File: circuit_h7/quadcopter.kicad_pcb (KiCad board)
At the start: 4 copper layers, 37.5 x 37.5 mm, 108 parts, among them J1 Conn_01x04_Male, J10 Conn_01x01_Female, J11 Conn_01x04_Male, J12 Conn_01x04_Male, J13 Conn_01x01_Female, J14 Conn_01x01_Female, J16 Conn_01x01_Female, J17 Conn_01x01_Female, J18 USB_C_Receptacle_USB2.0, J19 Conn_01x08_Male, J2 Conn_01x01_Female, J21 Conn_01x01_Female, J22 Conn_01x01_Female, J23 Conn_01x01_Female, J24 Conn_01x01_Female, J25 Conn_01x01_Female, J26 Conn_01x01_Female, J28 Conn_01x01_Female, J29 Conn_01x01_Female, J3 Conn_01x01_Female, J30 Conn_01x01_Female, J31 Conn_01x01_Female, J32 Conn_01x01_Female, J33 Conn_01x01_Female, J37 Conn_01x01_Female, J4 Conn_01x01_Female, J40 Conn_01x01_Female, J41 Conn_01x01_Female, J42 Conn_01x01_Female, J43 Conn_01x01_Female, J44 Conn_01x01_Female, J45 Conn_01x01_Female, J47 Conn_01x01_Female, J48 Conn_01x01_Female, J49 Conn_01x01_Female, J5 Conn_Coaxial, J50 Conn_01x01_Female, J6 Conn_01x06_Male, J7 Conn_01x01_Female, J8 Conn_01x01_Female, J9 Conn_01x01_Female, SW1 SW_DIP_x01, U1 STM32H723VGH6, U2 ICM-42605, U3 DPS310, U4 3V3, U5 EUP3458 1.2A, 30V max input, 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, U6 2450FM07D0034T, U7 W25Q80DVUXIE TR (16M), U8 SX1281, U9 5v, 500mA, Y1 16M, Y2 52Mhz, 12pF

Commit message: More work on routing
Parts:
- added J15: Conn_01x01_Female, TestPoint:TestPoint_Pad_2.0x2.0mm, B.Cu at (138.8, 97.2)
- moved R16 34.8 mm to (147.5, 85.2)
- moved R18 33.5 mm to (147.5, 86.2)
- moved R14 25.2 mm to (150.2, 95.5)
- moved R13 23.7 mm to (152.2, 95.5), turned to 0 degrees
- moved J12 21.1 mm to (141.6, 75.4)
- moved C2 16.2 mm to (147.3, 90.6), turned to -90 degrees
- moved U3 15.3 mm to (144.8, 90.6), turned to 0 degrees
- moved C5 15.1 mm to (142.3, 90.6), turned to 90 degrees
- moved J32 5.13 mm to (135.2, 97.2)
- moved C10 0.10 mm to (134.0, 78.6)
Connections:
- U1 pad G4: /IMU_INTERRUPT -> /CS_IMU
- U1 pad K8: /CS_IMU -> /IMU_INTERRUPT
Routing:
- net +10V: track 18.8 -> 52.3 mm
- net /USB_DN: track 0.00 -> 22.6 mm, vias 0 -> 2
- net /USB_DP: track 0.00 -> 21.5 mm, vias 0 -> 2
- net /BATT_DIV: track 0.00 -> 19.9 mm, vias 0 -> 2
- net /IMU_pwr: track 13.9 -> 32.7 mm, vias 0 -> 1
- net /UART3_RX: track 1.10 -> 16.1 mm
- net /BOOT0: track 0.00 -> 14.4 mm, vias 0 -> 2
- net /CUR_DIV: track 0.00 -> 13.8 mm, vias 0 -> 2
- net +3V3: track 17.4 -> 31.0 mm, vias 3 -> 10
- net /CS_ELRS: track 0.00 -> 13.4 mm, vias 0 -> 2
- net /ELRS_BUSY: track 0.00 -> 13.0 mm, vias 0 -> 2
- net GND: track 17.7 -> 30.0 mm, vias 8 -> 37
- net /SCL2: track 0.00 -> 12.2 mm, vias 0 -> 2
- net /SDA2: track 0.00 -> 10.9 mm, vias 0 -> 2
- net +5V: track 9.57 -> 19.0 mm, vias 2 -> 4
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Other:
- board text added: "I2C"

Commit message: More work on BF pid
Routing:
- net /UART2_RX: track 1.43 -> 20.0 mm, vias 1 -> 2
- net /UART2_TX: track 0.78 -> 14.9 mm, vias 1 -> 2
- net /IMU_pwr: track 32.7 -> 37.3 mm, vias 1 -> 2
- net GND: track 30.0 -> 33.7 mm, vias 37 -> 44
- net /USB_DN: track 22.6 -> 24.9 mm
- net /USB_DP: track 21.5 -> 23.7 mm
- net +3V3: track 31.0 -> 30.2 mm, vias 10 -> 12

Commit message: More work on board. Removed motor args from set power fns
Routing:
- net /UART1_RX: track 1.43 -> 57.1 mm, vias 1 -> 6
- net /UART4_TX: track 0.00 -> 31.4 mm, vias 0 -> 2
- net /UART4_RX: track 0.00 -> 26.3 mm, vias 0 -> 2
- net /SDA2: track 10.9 -> 28.5 mm, vias 2 -> 3
- net GND: track 33.7 -> 41.5 mm, vias 44 -> 52
- net +3V3: track 30.2 -> 35.5 mm, vias 12 -> 13
- net /MISO_2: track 14.1 -> 16.2 mm
- net +10V: track 52.3 -> 53.2 mm
- net /USB_DN: track 24.9 -> 24.2 mm

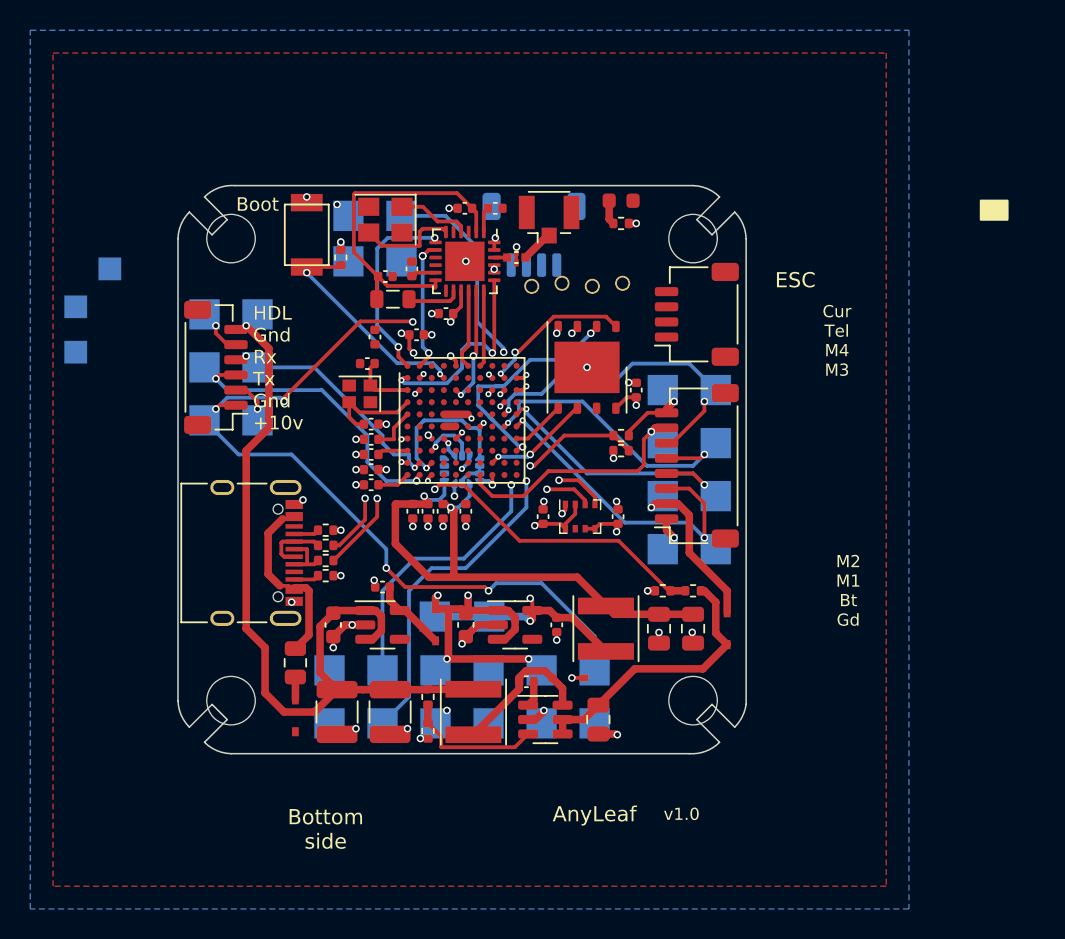
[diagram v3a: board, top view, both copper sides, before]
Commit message: Added link stats to preflight
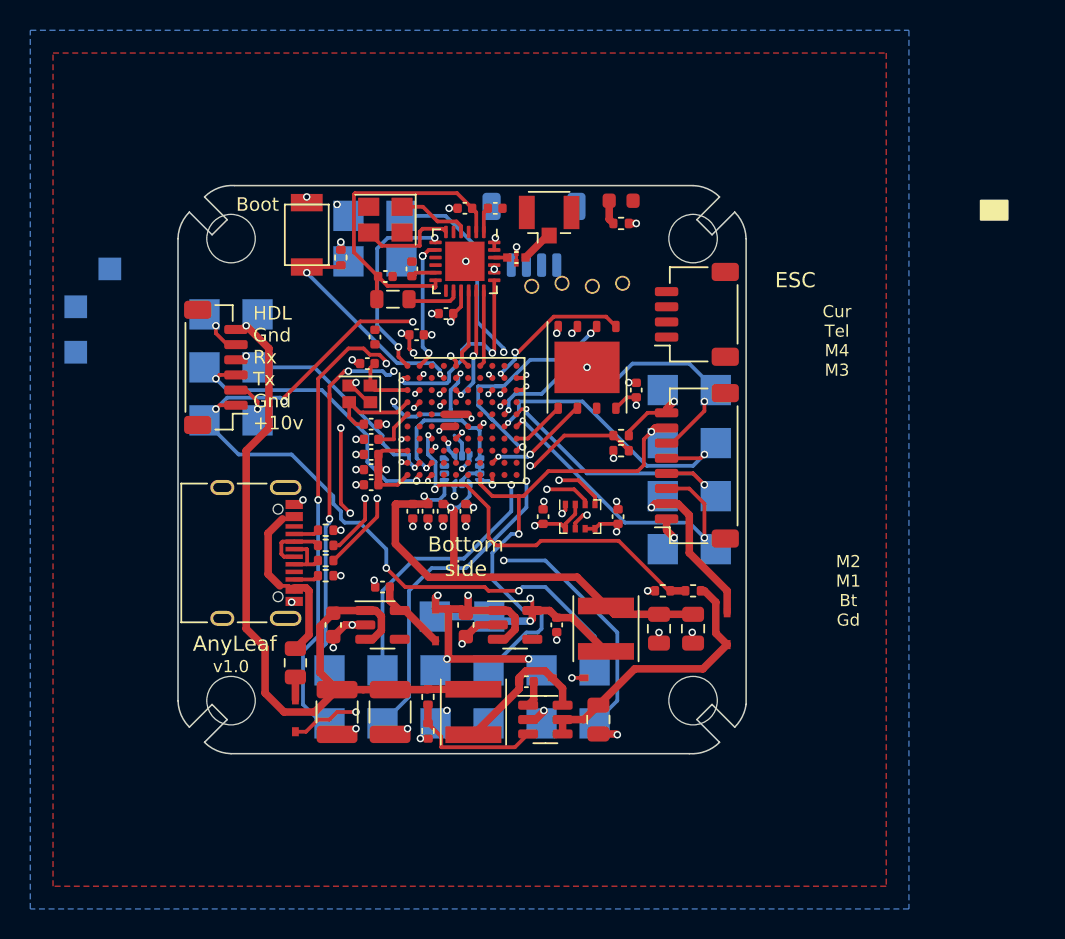
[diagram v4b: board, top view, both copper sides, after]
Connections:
- J14 pad 1: /UART5_RX -> /UART8_RX
- J2 pad 1: /UART5_TX -> /UART8_TX
- U1 pad C4: unconnected-(U1-PadC4) -> /UART8_TX
- U1 pad D4: unconnected-(U1-PadD4) -> /UART8_RX
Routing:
- net /UART1_TX: track 0.00 -> 45.6 mm, vias 0 -> 5
- net /UART8_TX: track 0.00 -> 35.5 mm, vias 0 -> 3
- net /UART8_RX: track 0.00 -> 28.6 mm, vias 0 -> 4
- net /UART3_RX: track 16.1 -> 32.4 mm, vias 1 -> 2
- net +5V: track 19.0 -> 31.0 mm, vias 4 -> 5
- net +3V3: track 35.5 -> 45.4 mm, vias 13 -> 16
- net /BATT_DIV: track 19.9 -> 25.1 mm
- net GND: track 41.5 -> 45.9 mm, vias 52 -> 55
- net /SCK_1: track 3.61 -> 1.90 mm

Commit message: H7 fixes
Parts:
- added C32: 12p, Capacitor_SMD:C_0402_1005Metric, F.Cu at (158.2, 65.0)
- added C33: 6.8p, Capacitor_SMD:C_0402_1005Metric, F.Cu at (158.3, 63.0)
- added C34: 1u 25v, Capacitor_SMD:C_0402_1005Metric, F.Cu at (147.8, 62.0)
- added C35: 100n, Capacitor_SMD:C_0402_1005Metric, F.Cu at (155.2, 67.0)
- added C36: 10u, Capacitor_SMD:C_0402_1005Metric, F.Cu at (155.4, 65.0)
- added C37: 1u 25v, Capacitor_SMD:C_0402_1005Metric, F.Cu at (146.2, 64.2)
- added D6: LED, LED_SMD:LED_0603_1608Metric, F.Cu at (151.2, 65.2)
- added J20: Conn_01x01_Female, TestPoint:TestPoint_Pad_1.0x1.0mm, B.Cu at (149.5, 77.8)
- added R6: 10k, Resistor_SMD:R_0402_1005Metric, F.Cu at (155.4, 63.0)
- added R9: 3.3k, Resistor_SMD:R_0402_1005Metric, F.Cu at (172.7, 70.2)
- added U10: ESP8285, Package_DFN_QFN:QFN-32-1EP_5x5mm_P0.5mm_EP3.45x3.45mm, F.Cu at (145.2, 76.2)
- added Y3: 40M, Crystal:Crystal_SMD_2016-4Pin_2.0x1.6mm, F.Cu at (150.8, 77.0)
- J1: value Conn_01x04_Male -> Conn_01x01_Female; footprint Connector_JST:JST_SH_SM04B-SRSS-TB_1x04-1MP_P1.00mm_Horizontal -> TestPoint:TestPoint_Pad_1.0x1.0mm; moved to B.Cu
- J11: footprint Connector_JST:JST_SH_SM04B-SRSS-TB_1x04-1MP_P1.00mm_Horizontal -> Connector_JST:JST_GH_SM04B-GHS-TB_1x04-1MP_P1.25mm_Horizontal
- J19: footprint Connector_JST:JST_SH_SM08B-SRSS-TB_1x08-1MP_P1.00mm_Horizontal -> Connector_JST:JST_GH_SM08B-GHS-TB_1x08-1MP_P1.25mm_Horizontal
- J6: footprint Connector_JST:JST_SH_BM06B-SRSS-TB_1x06-1MP_P1.00mm_Vertical -> Connector_JST:JST_GH_SM06B-GHS-TB_1x06-1MP_P1.25mm_Horizontal
- moved J12 38.7 mm to (110.8, 98.8)
- moved J1 3.35 mm to (149.5, 75.8), turned to 180 degrees
- moved U7 2.25 mm to (145.2, 83.0)
- moved R18 2.14 mm to (145.5, 87.0)
- moved J11 1.77 mm to (143.5, 72.2)
- moved R16 1.75 mm to (147.5, 87.0)
- moved J6 1.06 mm to (121.5, 81.5), turned to -90 degrees
- moved C23 0.35 mm to (148.8, 82.5)
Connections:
- J1 pad 1: /SCL1 -> /TX_ELRS
- U1 pad A1: /ELRS_BUSY -> unconnected-(U1-PadA1)
- U1 pad A2: /ELRS_DIO -> unconnected-(U1-PadA2)
- U1 pad A6: /MISO_3 -> unconnected-(U1-PadA6)
- U1 pad A7: /SCK_3 -> unconnected-(U1-PadA7)
- U1 pad B1: /CS_ELRS -> unconnected-(U1-PadB1)
- U1 pad C5: /MOSI_3 -> unconnected-(U1-PadC5)
- U8 pad 16: /MISO_3 -> /MISO_ELRS
- U8 pad 17: /MOSI_3 -> /MOSI_ELRS
- U8 pad 18: /SCK_3 -> /SCK_ELRS
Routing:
- net /SDA1: track 0.00 -> 14.4 mm, vias 0 -> 1
- net unconnected-(U1-PadA1): track 0.00 -> 13.0 mm, vias 0 -> 2
- net /ELRS_BUSY: track 13.0 -> 0.00 mm, vias 2 -> 0
- net /MISO_ELRS: track 0.00 -> 9.91 mm, vias 0 -> 3
- net /SCL1: track 0.00 -> 9.12 mm, vias 0 -> 1
- net /CS_ELRS: track 13.4 -> 4.66 mm
- net unconnected-(U1-PadA2): track 0.00 -> 8.68 mm, vias 0 -> 3
- net /ELRS_DIO: track 8.68 -> 0.00 mm, vias 3 -> 0
- net unconnected-(U1-PadB1): track 0.00 -> 8.57 mm, vias 0 -> 2
- net /CS_FLASH: track 10.2 -> 2.26 mm
- net /MOSI_3: track 7.77 -> 0.00 mm, vias 2 -> 0
- net /CUR_DIV: track 13.8 -> 7.26 mm
- net /MISO_2: track 16.2 -> 10.1 mm, vias 2 -> 1
- net /SCK_ELRS: track 0.00 -> 6.09 mm
- net /MOSI_ELRS: track 0.00 -> 5.71 mm
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
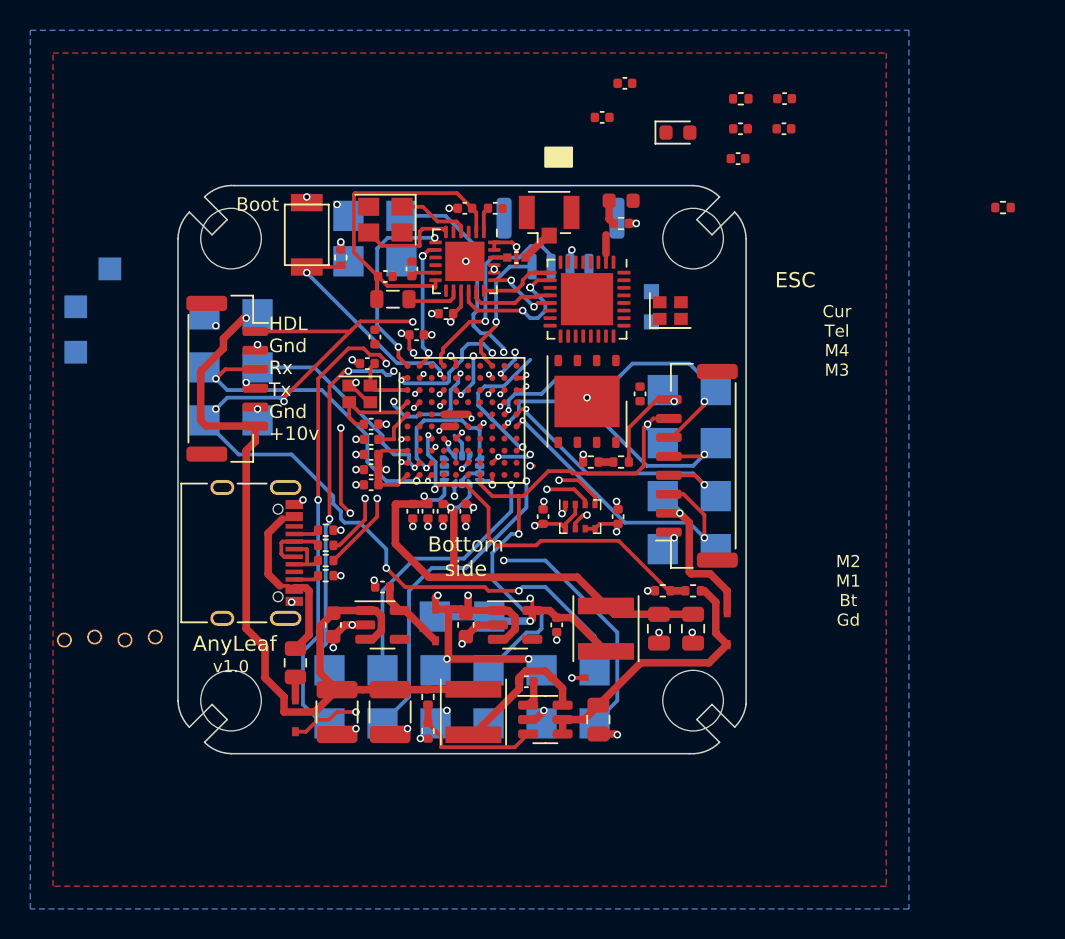
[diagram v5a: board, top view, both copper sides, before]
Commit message: Major refactor of motor timer logic, to reduce DRY between G4 and H7
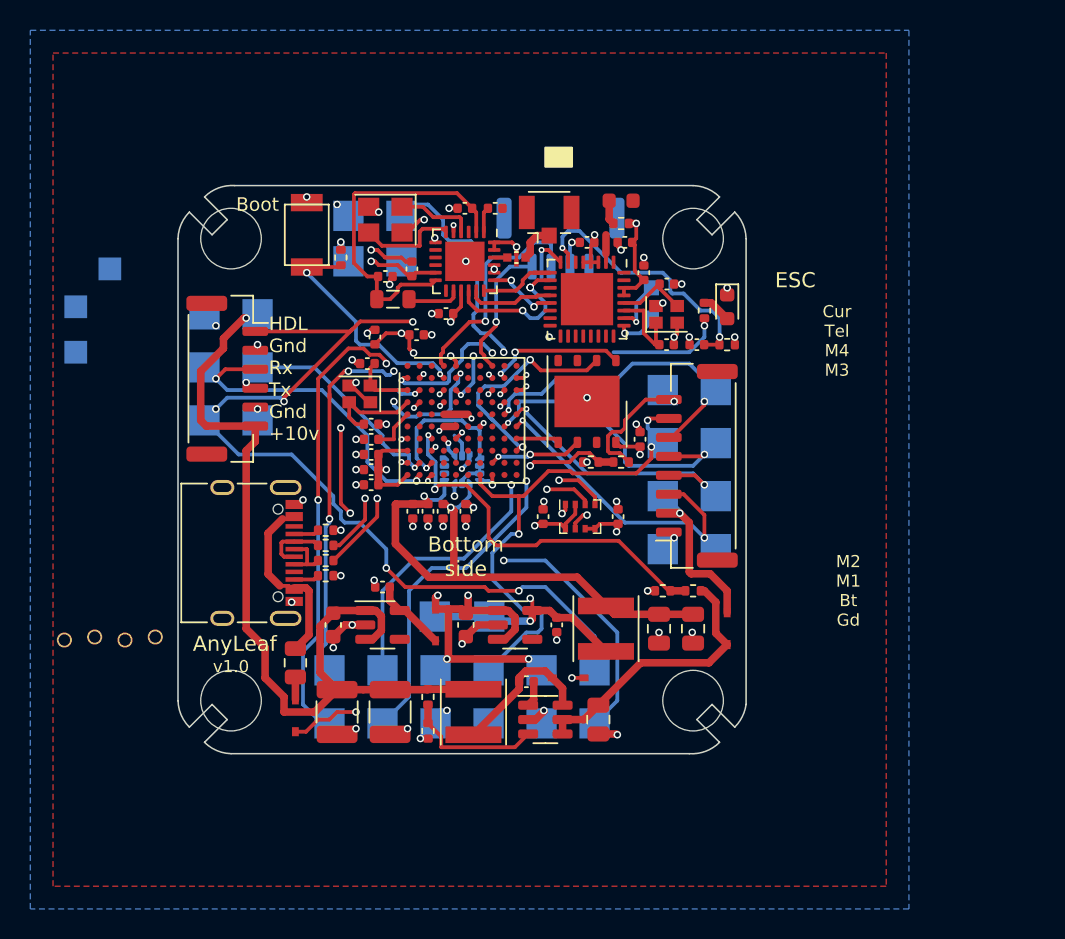
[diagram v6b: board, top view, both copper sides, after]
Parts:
- C32: value 12p -> 10p
- C33: value 6.8p -> 10p
- moved R9 20.9 mm to (153.0, 77.0), turned to -90 degrees
- moved C34 17.9 mm to (152.5, 79.2), turned to 180 degrees
- moved R6 16.3 mm to (154.5, 79.2)
- moved C32 16.2 mm to (150.5, 79.2), turned to 180 degrees
- moved C33 14.5 mm to (150.5, 75.2), turned to 180 degrees
- moved D6 12.0 mm to (154.5, 76.8), turned to -90 degrees
- moved C36 10.7 mm to (147.8, 72.5)
- moved C35 9.77 mm to (149.0, 74.5), turned to -90 degrees
- moved C37 8.31 mm to (145.2, 72.5), turned to 180 degrees
- moved C23 3.00 mm to (148.8, 85.5)
- moved Y3 0.35 mm to (150.5, 77.2)
- moved J1 0.25 mm to (149.5, 75.5)
- moved J20 0.25 mm to (149.5, 77.5)
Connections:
- U10 pad 32: /CS_ELRS -> unconnected-(U10-Pad32)
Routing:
- net Net-(R6-Pad1): track 0.00 -> 18.0 mm, vias 0 -> 2
- net +3V3: track 43.3 -> 60.2 mm, vias 15 -> 19
- net GND: track 42.4 -> 57.5 mm, vias 54 -> 68
- net unconnected-(U1-PadA1): track 13.0 -> 0.00 mm, vias 2 -> 0
- net Net-(U10-Pad8): track 0.00 -> 11.2 mm, vias 0 -> 2
- net unconnected-(U1-PadA2): track 8.68 -> 0.00 mm, vias 3 -> 0
- net /RX_ELRS: track 0.00 -> 7.94 mm, vias 0 -> 2
- net /CS_FLASH: track 2.26 -> 9.22 mm
- net Net-(C32-Pad2): track 0.00 -> 5.75 mm
- net /MISO_2: track 10.1 -> 15.0 mm, vias 1 -> 2
- net /CUR_DIV: track 7.26 -> 12.1 mm
- net Net-(U10-Pad28): track 0.00 -> 4.80 mm
- net /TX_ELRS: track 0.00 -> 3.58 mm, vias 0 -> 1
- net /SCK_2: track 2.78 -> 6.23 mm
- net /MOSI_2: track 0.00 -> 2.85 mm
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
